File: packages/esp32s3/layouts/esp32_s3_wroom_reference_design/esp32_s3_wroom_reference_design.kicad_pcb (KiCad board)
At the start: 2 copper layers, 7 parts

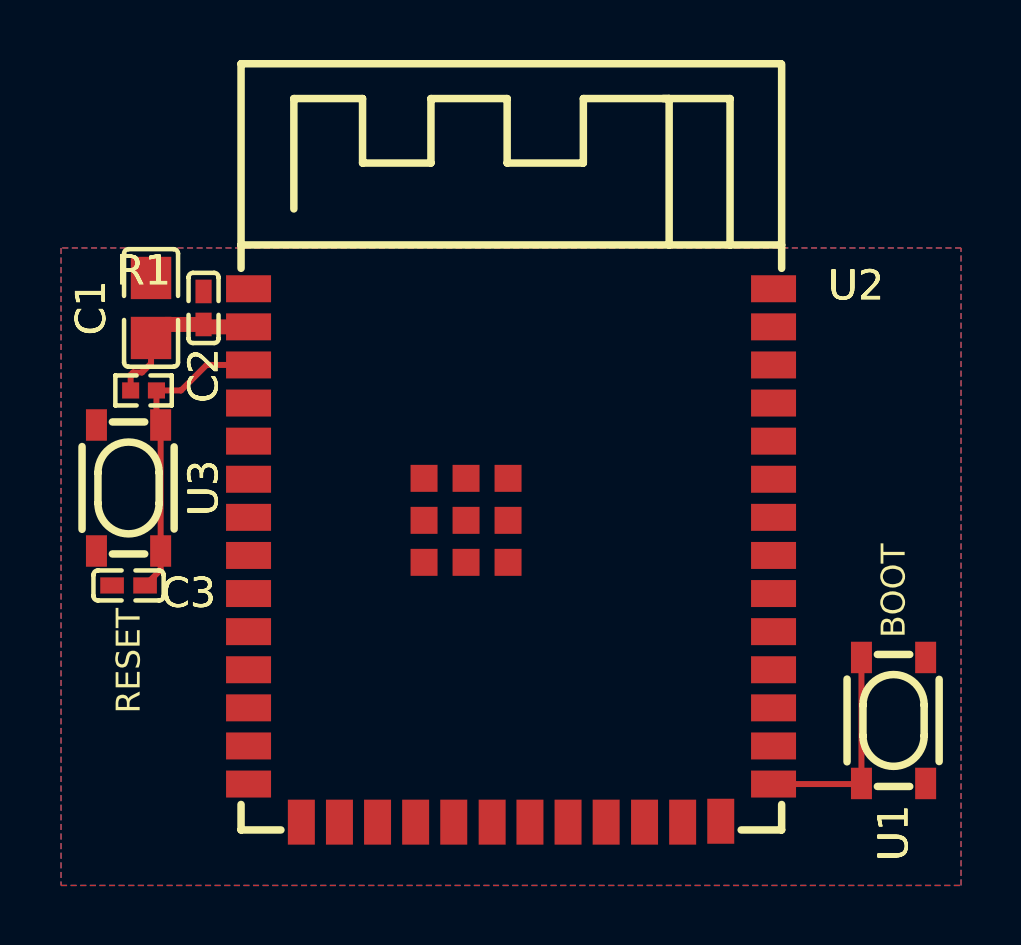
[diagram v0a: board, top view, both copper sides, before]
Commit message: Build all packages without designators on silkscreen.
Also disable fail_on_drc and enable keep_picked_parts for build
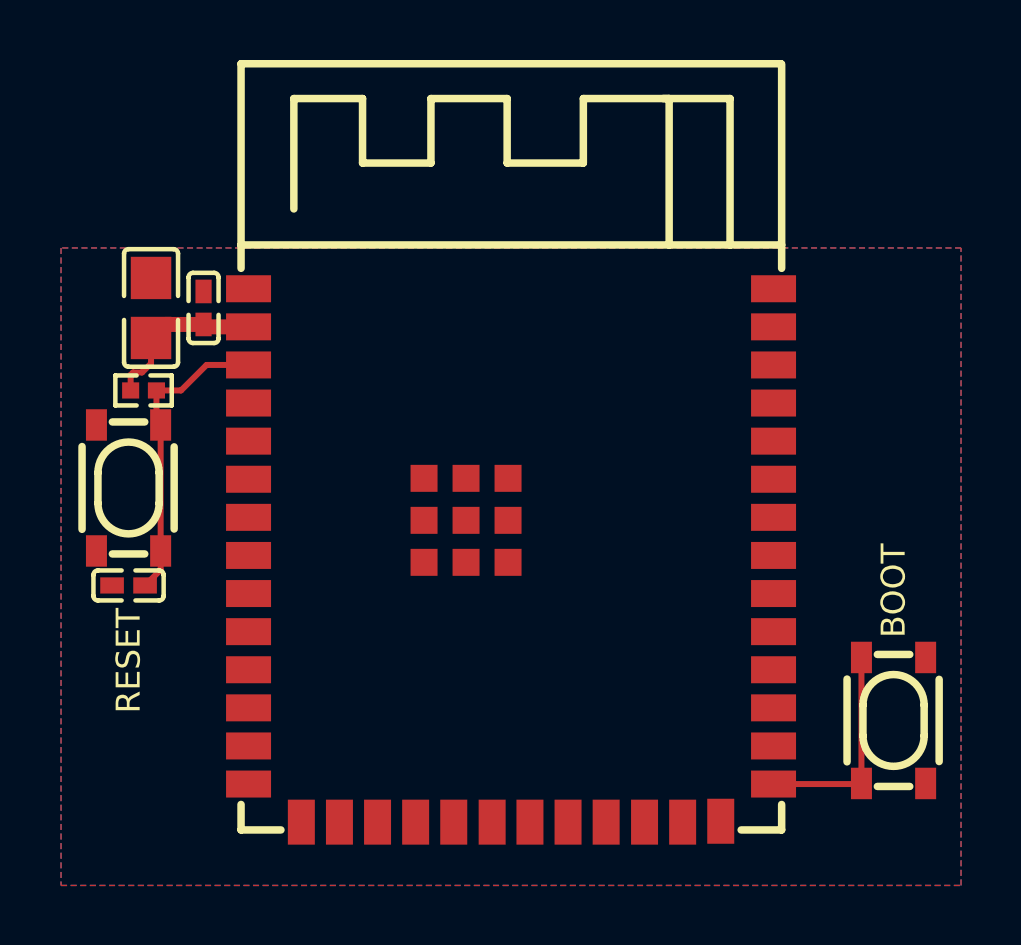
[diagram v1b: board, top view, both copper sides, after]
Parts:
- C1: value 10µF ±10% 25V X5R -> 100nF ±10% 50V X7R
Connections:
- U2 pad 10: line-1 -> line-13
- U2 pad 11: line-13 -> line-6
- U2 pad 12: line-25 -> line-1
- U2 pad 13: line-8 -> line-7
- U2 pad 14: line-18 -> line-20
- U2 pad 15: line-4 -> line-21
- U2 pad 16: line-32 -> line-18
- U2 pad 17: line-15 -> line-24
- U2 pad 18: line-17 -> line-30
- U2 pad 19: line-34 -> line-8
- U2 pad 20: line-27 -> line-32
- U2 pad 21: line-29 -> line-23
- U2 pad 22: line-19 -> line-9
- U2 pad 23: line-23 -> line-15
- U2 pad 24: line-20 -> line-33
- U2 pad 25: line-31 -> line-26
- U2 pad 26: line-3 -> line-14
- U2 pad 28: line -> line-19
- U2 pad 29: line-9 -> line-34
- U2 pad 30: line-33 -> line
- U2 pad 31: line-11 -> line-5
- U2 pad 32: line-7 -> line-12
- U2 pad 33: line-16 -> line-27
- U2 pad 34: line-21 -> line-4
- U2 pad 35: line-22 -> line-3
- U2 pad 36: line-2 -> line-10
- U2 pad 37: line-10 -> line-29
- U2 pad 38: line-5 -> line-31
- U2 pad 39: line-6 -> line-16
- U2 pad 4: line-12 -> line-28
- U2 pad 5: line-30 -> line-22
- U2 pad 6: line-14 -> line-25
- U2 pad 7: line-24 -> line-11
- U2 pad 8: line-26 -> line-2
- U2 pad 9: line-28 -> line-17

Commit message: Rebuild modules
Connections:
- U2 pad 10: line-13 -> line-28
- U2 pad 11: line-6 -> line-29
- U2 pad 12: line-1 -> line-9
- U2 pad 13: line-7 -> line-26
- U2 pad 14: line-20 -> line-15
- U2 pad 16: line-18 -> line
- U2 pad 18: line-30 -> line-33
- U2 pad 19: line-8 -> line-6
- U2 pad 20: line-32 -> line-13
- U2 pad 21: line-23 -> line-1
- U2 pad 22: line-9 -> line-23
- U2 pad 23: line-15 -> line-25
- U2 pad 24: line-33 -> line-32
- U2 pad 25: line-26 -> line-11
- U2 pad 26: line-14 -> line-3
- U2 pad 28: line-19 -> line-2
- U2 pad 30: line -> line-10
- U2 pad 31: line-5 -> line-22
- U2 pad 32: line-12 -> line-7
- U2 pad 33: line-27 -> line-14
- U2 pad 34: line-4 -> line-8
- U2 pad 35: line-3 -> line-27
- U2 pad 36: line-10 -> line-17
- U2 pad 37: line-29 -> line-16
- U2 pad 38: line-31 -> line-5
- U2 pad 39: line-16 -> line-30
- U2 pad 4: line-28 -> line-31
- U2 pad 5: line-22 -> line-19
- U2 pad 6: line-25 -> line-20
- U2 pad 7: line-11 -> line-18
- U2 pad 8: line-2 -> line-12
- U2 pad 9: line-17 -> line-4
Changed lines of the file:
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@@
     )
     (net 0 "")
-    (net 1 "line-7")
-    (net 2 "line-17")
-    (net 3 "line-23")
-    (net 4 "line-32")
-    (net 5 "line-1")
-    (net 6 "line-11")
-    (net 7 "line-12")
-    (net 8 "line-6")
-    (net 9 "line-5")
-    (net 10 "line-4")
-    (net 11 "line-19")
-    (net 12 "line-13")
-    (net 13 "line-27")
+    (net 1 "line-26")
+    (net 2 "line-4")
+    (net 3 "line-1")
+    (net 4 "line-13")
+    (net 5 "line-9")
+    (net 6 "line-18")
+    (net 7 "line-7")
+    (net 8 "line-29")
+    (net 9 "line-22")
+    (net 10 "line-8")
+    (net 11 "line-2")
+    (net 12 "line-28")
+    (net 13 "line-14")
     (net 14 "out")
-    (net 15 "line-16")
-    (net 16 "line-29")
-    (net 17 "line-28")
+    (net 15 "line-30")
+    (net 16 "line-16")
+    (net 17 "line-31")
     (net 18 "line-34")
-    (net 19 "line-14")
-    (net 20 "line-20")
-    (net 21 "line-15")
-    (net 22 "line")
-    (net 23 "line-8")
-    (net 24 "line-10")
-    (net 25 "line-3")
-    (net 26 "line-26")
+    (net 19 "line-3")
+    (net 20 "line-15")
+    (net 21 "line-25")
+    (net 22 "line-10")
+    (net 23 "line-6")
+    (net 24 "line-17")
+    (net 25 "line-27")
+    (net 26 "line-11")
     (net 27 "hv")
-    (net 28 "line-33")
-    (net 29 "line-30")
-    (net 30 "line-2")
+    (net 28 "line-32")
+    (net 29 "line-33")
+    (net 30 "line-12")
     (net 31 "line-21")
-    (net 32 "line-31")
+    (net 32 "line-5")
     (net 33 "line-24")
-    (net 34 "line-18")
-    (net 35 "line-22")
-    (net 36 "line-25")
-    (net 37 "line-9")
+    (net 34 "line")
+    (net 35 "line-19")
+    (net 36 "line-20")
+    (net 37 "line-23")
     (net 38 "gnd")
     (net 41 "in")
@@
             (size 1.5 0.9)
             (layers "F.Cu" "F.Mask" "F.Paste")
-            (net 17 "line-28")
+            (net 17 "line-31")
         )
         (pad "5" smd rect
@@
             (size 1.5 0.9)
             (layers "F.Cu" "F.Mask" "F.Paste")
-            (net 35 "line-22")
+            (net 35 "line-19")
         )
         (pad "6" smd rect
@@
             (size 1.5 0.9)
             (layers "F.Cu" "F.Mask" "F.Paste")
-            (net 36 "line-25")
+            (net 36 "line-20")
         )
         (pad "7" smd rect
@@
             (size 1.5 0.9)
             (layers "F.Cu" "F.Mask" "F.Paste")
-            (net 6 "line-11")
+            (net 6 "line-18")
         )
         (pad "8" smd rect
@@
             (size 1.5 0.9)
             (layers "F.Cu" "F.Mask" "F.Paste")
-            (net 30 "line-2")
+            (net 30 "line-12")
         )
         (pad "9" smd rect
@@
             (size 1.5 0.9)
             (layers "F.Cu" "F.Mask" "F.Paste")
-            (net 2 "line-17")
+            (net 2 "line-4")
         )
         (pad "10" smd rect
@@
             (size 1.5 0.9)
             (layers "F.Cu" "F.Mask" "F.Paste")
-            (net 12 "line-13")
+            (net 12 "line-28")
         )
         (pad "11" smd rect
@@
             (size 1.5 0.9)
             (layers "F.Cu" "F.Mask" "F.Paste")
-            (net 8 "line-6")
+            (net 8 "line-29")
         )
         (pad "12" smd rect
@@
             (size 1.5 0.9)
             (layers "F.Cu" "F.Mask" "F.Paste")
-            (net 5 "line-1")
+            (net 5 "line-9")
         )
         (pad "13" smd rect
@@
             (size 1.5 0.9)
             (layers "F.Cu" "F.Mask" "F.Paste")
-            (net 1 "line-7")
+            (net 1 "line-26")
         )
         (pad "14" smd rect
@@
             (size 1.5 0.9)
             (layers "F.Cu" "F.Mask" "F.Paste")
-            (net 20 "line-20")
+            (net 20 "line-15")
         )
         (pad "15" smd rect
@@
             (size 1.5 0.9)
             (layers "F.Cu" "F.Mask" "F.Paste")
-            (net 34 "line-18")
+            (net 34 "line")
         )
         (pad "17" smd rect
@@
             (size 1.5 0.9)
             (layers "F.Cu" "F.Mask" "F.Paste")
-            (net 29 "line-30")
+            (net 29 "line-33")
         )
         (pad "19" smd rect
@@
             (size 1.5 0.9)
             (layers "F.Cu" "F.Mask" "F.Paste")
-            (net 23 "line-8")
+            (net 23 "line-6")
         )
         (pad "20" smd rect
@@
             (size 1.5 0.9)
             (layers "F.Cu" "F.Mask" "F.Paste")
-            (net 4 "line-32")
+            (net 4 "line-13")
         )
         (pad "21" smd rect
@@
             (size 1.5 0.9)
             (layers "F.Cu" "F.Mask" "F.Paste")
-            (net 3 "line-23")
+            (net 3 "line-1")
         )
         (pad "22" smd rect
@@
             (size 1.5 0.9)
             (layers "F.Cu" "F.Mask" "F.Paste")
-            (net 37 "line-9")
+            (net 37 "line-23")
         )
         (pad "23" smd rect
@@
             (size 1.5 0.9)
             (layers "F.Cu" "F.Mask" "F.Paste")
-            (net 21 "line-15")
+            (net 21 "line-25")
         )
         (pad "24" smd rect
@@
             (size 1.5 0.9)
             (layers "F.Cu" "F.Mask" "F.Paste")
-            (net 28 "line-33")
+            (net 28 "line-32")
         )
         (pad "25" smd rect
@@
             (size 1.5 0.9)
             (layers "F.Cu" "F.Mask" "F.Paste")
-            (net 26 "line-26")
+            (net 26 "line-11")
         )
         (pad "26" smd rect
@@
             (size 1.5 0.9)
             (layers "F.Cu" "F.Mask" "F.Paste")
-            (net 19 "line-14")
+            (net 19 "line-3")
         )
         (pad "27" smd rect
@@
             (size 1.5 0.9)
             (layers "F.Cu" "F.Mask" "F.Paste")
-            (net 11 "line-19")
+            (net 11 "line-2")
         )
         (pad "29" smd rect
@@
             (size 1.5 0.9)
             (layers "F.Cu" "F.Mask" "F.Paste")
-            (net 22 "line")
+            (net 22 "line-10")
         )
         (pad "31" smd rect
@@
             (size 1.5 0.9)
             (layers "F.Cu" "F.Mask" "F.Paste")
-            (net 9 "line-5")
+            (net 9 "line-22")
         )
         (pad "32" smd rect
@@
             (size 1.5 0.9)
             (layers "F.Cu" "F.Mask" "F.Paste")
-            (net 7 "line-12")
+            (net 7 "line-7")
         )
         (pad "33" smd rect
@@
             (size 1.5 0.9)
             (layers "F.Cu" "F.Mask" "F.Paste")
-            (net 13 "line-27")
+            (net 13 "line-14")
         )
         (pad "34" smd rect
@@
             (size 1.5 0.9)
             (layers "F.Cu" "F.Mask" "F.Paste")
-            (net 10 "line-4")
+            (net 10 "line-8")
         )
         (pad "35" smd rect
@@
             (size 1.5 0.9)
             (layers "F.Cu" "F.Mask" "F.Paste")
-            (net 25 "line-3")
+            (net 25 "line-27")
         )
         (pad "36" smd rect
@@
             (size 1.5 0.9)
             (layers "F.Cu" "F.Mask" "F.Paste")
-            (net 24 "line-10")
+            (net 24 "line-17")
         )
         (pad "37" smd rect
@@
             (size 1.5 0.9)
             (layers "F.Cu" "F.Mask" "F.Paste")
-            (net 16 "line-29")
+            (net 16 "line-16")
         )
         (pad "38" smd rect
@@
             (size 1.5 0.9)
             (layers "F.Cu" "F.Mask" "F.Paste")
-            (net 32 "line-31")
+            (net 32 "line-5")
         )
         (pad "39" smd rect
@@
             (size 1.5 0.9)
             (layers "F.Cu" "F.Mask" "F.Paste")
-            (net 15 "line-16")
+            (net 15 "line-30")
         )
         (pad "40" smd rect
